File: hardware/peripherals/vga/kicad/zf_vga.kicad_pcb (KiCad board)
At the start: 2 copper layers, 143 x 85 mm, 55 parts, among them J2 Z-FIGHTER Expansion Port, SW1 SW_DIP_x03, U1 4040, U10 74HC165, U11 AS6C6264, U12 74HC541, U13 74HC541, U14 74HC541, U2 4040, U3 GAL16V8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

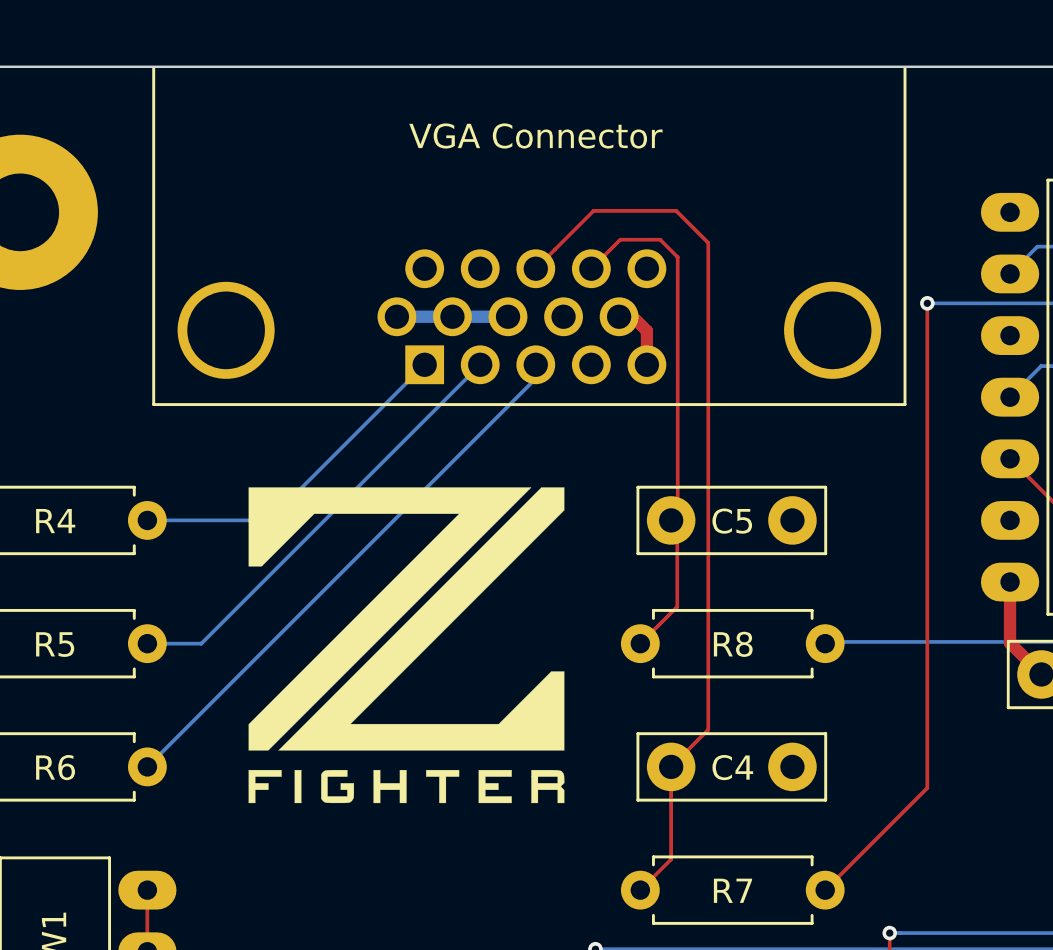
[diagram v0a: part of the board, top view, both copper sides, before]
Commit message: Replaced VGA connector footprint
KiCad library horizontal D-SUB 15 footprint uses incorrect pin spacing.
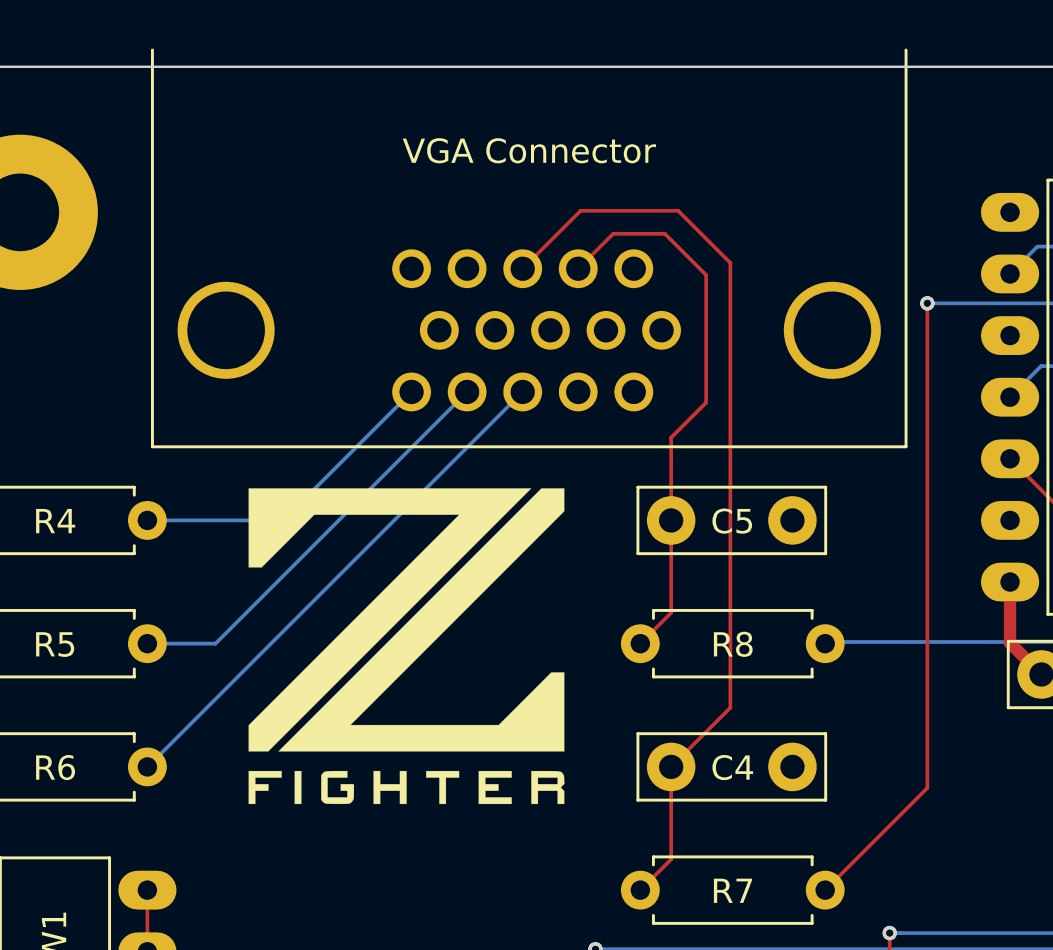
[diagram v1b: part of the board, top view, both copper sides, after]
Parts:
- VGA Connector: footprint Connector_Dsub:DSUB-15-HD_Female_Horizontal_P2.29x1.98mm_EdgePinOffset8.35mm_Housed_MountingHolesOffset10.89mm -> zf_vga:AHDF15A-KG-TAXB
- moved VGA Connector 13.6 mm to (113.6, 23.9), turned to 0 degrees
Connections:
- U11 pad 28: (no net) -> VCC
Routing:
- net VCC: track 72.0 -> 83.9 mm
- net (no net): track 12.0 -> 0.00 mm
- net GND: track 35.1 -> 26.6 mm
- net Net-(C5-Pad1): track 21.1 -> 22.9 mm
- net Net-(J3-Pad3): track 23.8 -> 22.0 mm
- net Net-(C4-Pad1): track 36.5 -> 37.8 mm
- net Net-(J3-Pad1): track 14.1 -> 13.1 mm
- net Net-(J3-Pad2): track 18.5 -> 17.5 mm
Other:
- board text added: "Z-FIGHTER VGA Module Rev. 0a @tangent3D 2022"
- board text removed: "Z-FIGHTER VGA Module Rev. 0 @tangent3D 2022"

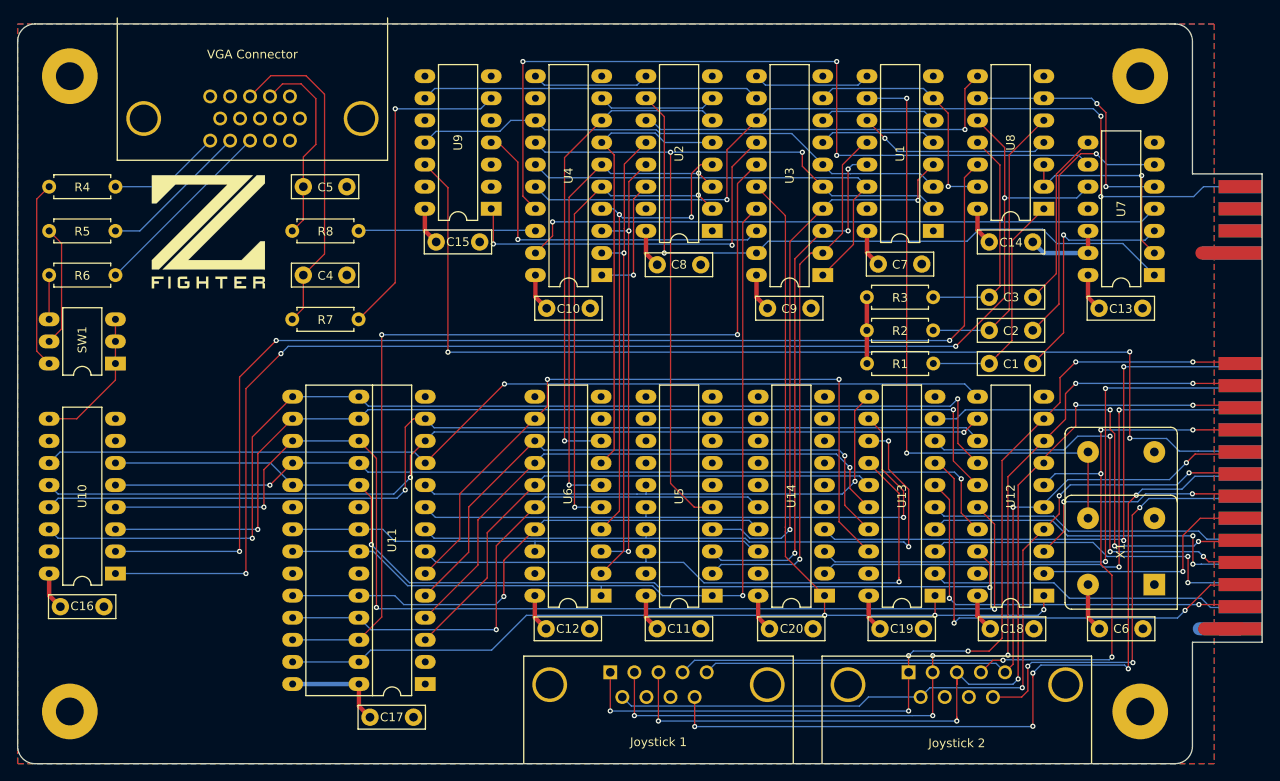
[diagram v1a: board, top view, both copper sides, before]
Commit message: VGA Module Rev. 1
Fixed noise issues, added pull-up resistor to DATARDY
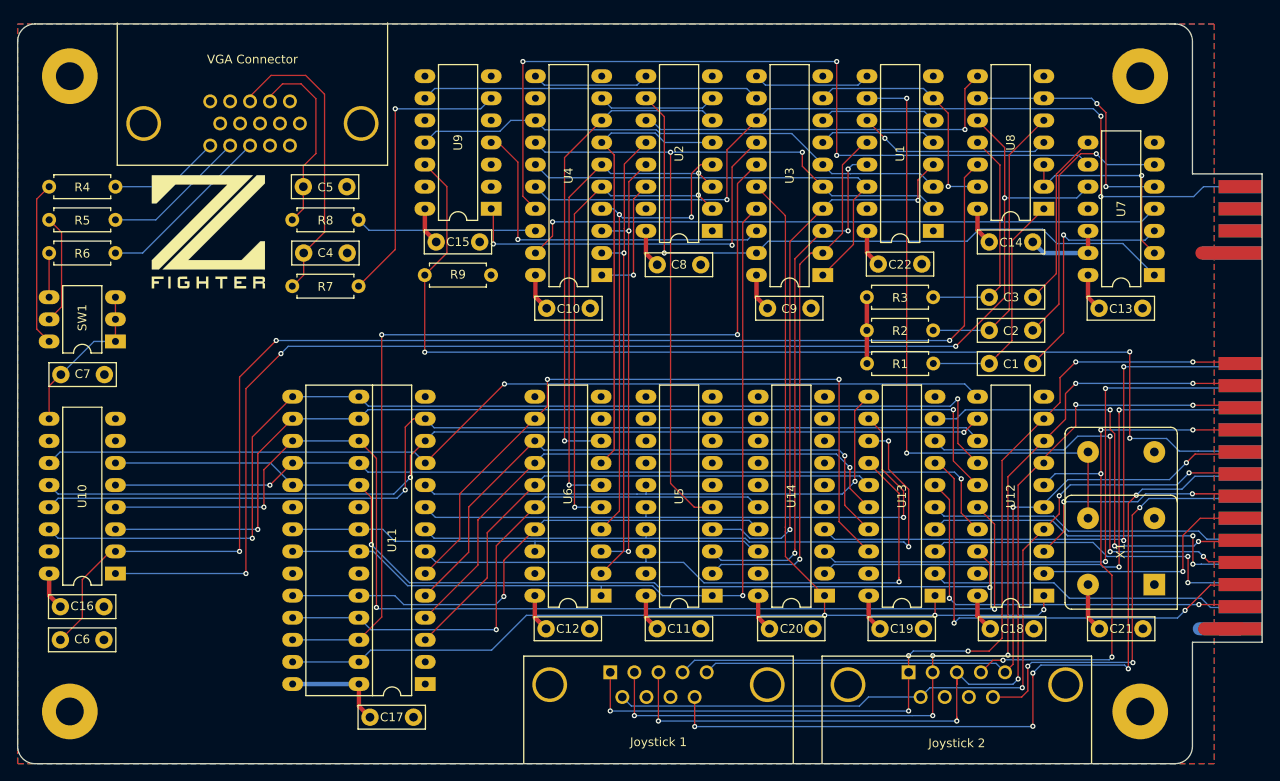
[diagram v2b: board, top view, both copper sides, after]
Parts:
- added C6: 470pF, Capacitor_THT:C_Disc_D7.5mm_W2.5mm_P5.00mm, F.Cu at (91.5, 95.3)
- added C7: 470pF, Capacitor_THT:C_Disc_D7.5mm_W2.5mm_P5.00mm, F.Cu at (96.6, 64.8)
- added R9: 1KΩ, Resistor_THT:R_Axial_DIN0207_L6.3mm_D2.5mm_P7.62mm_Horizontal, F.Cu at (141.0, 53.4)
- C4, C5: value C_Small -> 22pF
- R4, R5, R6, R7, R8: value R -> 75Ω
- moved C4 5.64 mm to (124.5, 50.8), turned to 180 degrees
- moved R7 3.81 mm to (125.8, 54.6)
- moved SW1 2.54 mm to (97.9, 61.0)
- moved R6 2.54 mm to (90.2, 50.8)
- moved R5 1.27 mm to (90.2, 47.0)
- moved R8 1.27 mm to (125.8, 47.0)
- moved VGA Connector 0.57 mm to (113.6, 24.5)
- renumbered C6 to C21, C7 to C22
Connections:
- C4 pad 1: Net-(C4-Pad1) -> GND
- C4 pad 2: GND -> Net-(C4-Pad2)
- R7 pad 2: Net-(C4-Pad1) -> Net-(C4-Pad2)
- U11 pad 28: VCC -> (no net)
- VGA Connector pad 13: Net-(C4-Pad1) -> Net-(C4-Pad2)
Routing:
- net Net-(C4-Pad1): track 37.8 -> 0.00 mm
- net Net-(C4-Pad2): track 0.00 -> 34.1 mm
- net #P1: track 139.1 -> 152.2 mm
- net VCC: track 83.9 -> 72.0 mm
- net (no net): track 0.00 -> 12.0 mm
- net #HSYNC: track 37.5 -> 33.7 mm
- net DATARDY: track 123.9 -> 127.5 mm
- net Net-(R4-Pad1): track 21.5 -> 19.0 mm
- net VIDOUT: track 16.4 -> 18.6 mm
- net Net-(J3-Pad3): track 22.0 -> 20.6 mm
- net Net-(C5-Pad1): track 22.9 -> 21.6 mm
- net Net-(R5-Pad1): track 13.9 -> 12.6 mm
- net Net-(J3-Pad2): track 17.5 -> 16.7 mm
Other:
- board text added: "Z-FIGHTER VGA Module Rev. 1 @tangent3D 2022"
- board text removed: "Z-FIGHTER VGA Module Rev. 0a @tangent3D 2022"

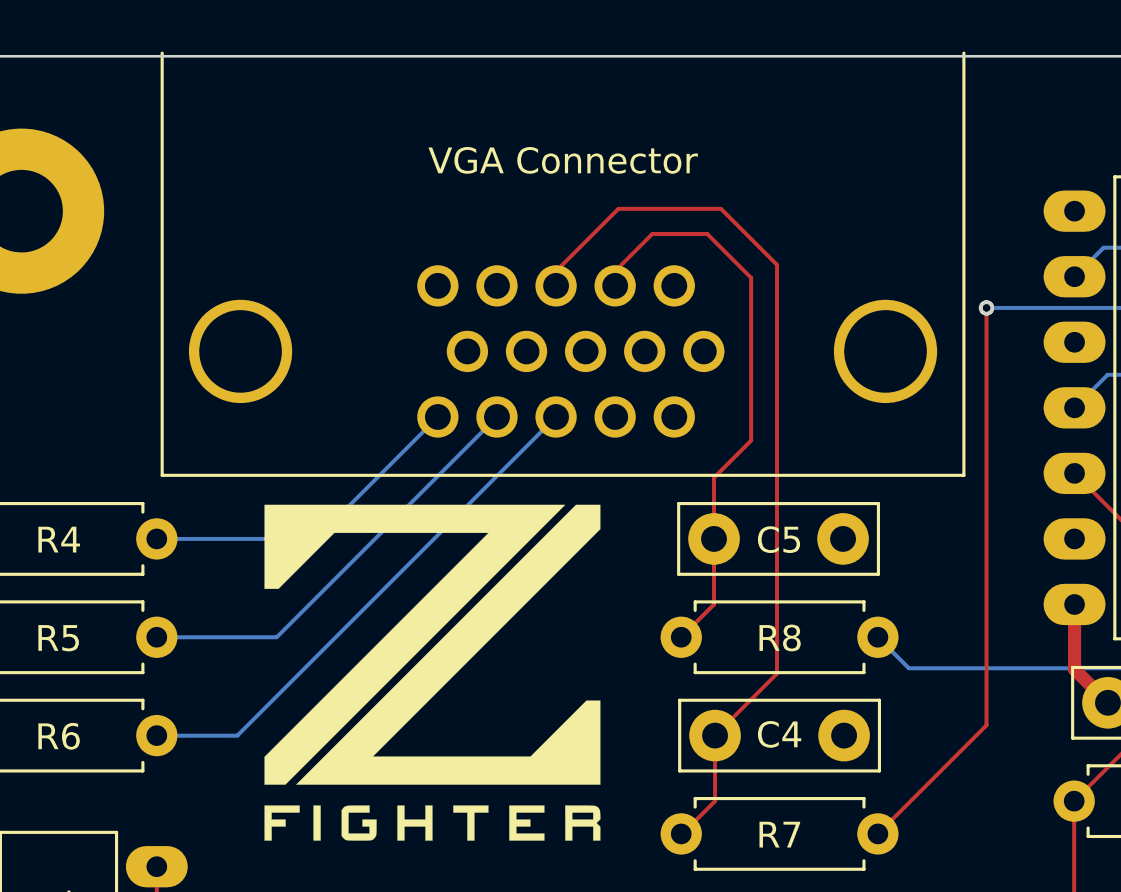
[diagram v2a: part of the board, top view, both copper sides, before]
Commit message: Moved VGA connector slightly
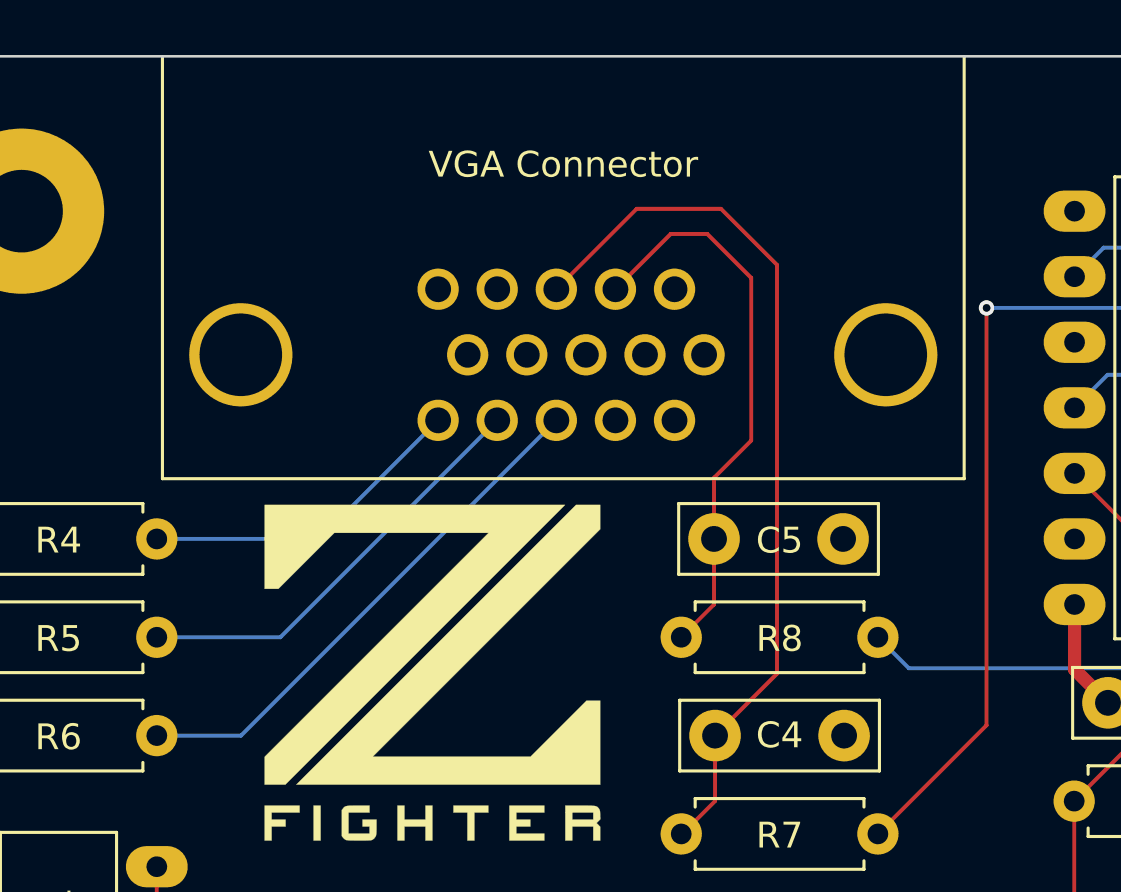
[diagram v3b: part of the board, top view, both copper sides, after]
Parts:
- moved VGA Connector 0.13 mm to (113.6, 24.6)
